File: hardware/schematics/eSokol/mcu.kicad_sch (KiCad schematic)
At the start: 16 parts, among them J1 DB25, J2 to HC-05, Q6 AO3400A, SW1 SW_LITTLE, U2 YAAJ_BluePill_SWD_Breakout, U3 TP4056, U5 AMS1117-5.0, U9 TCRT5000

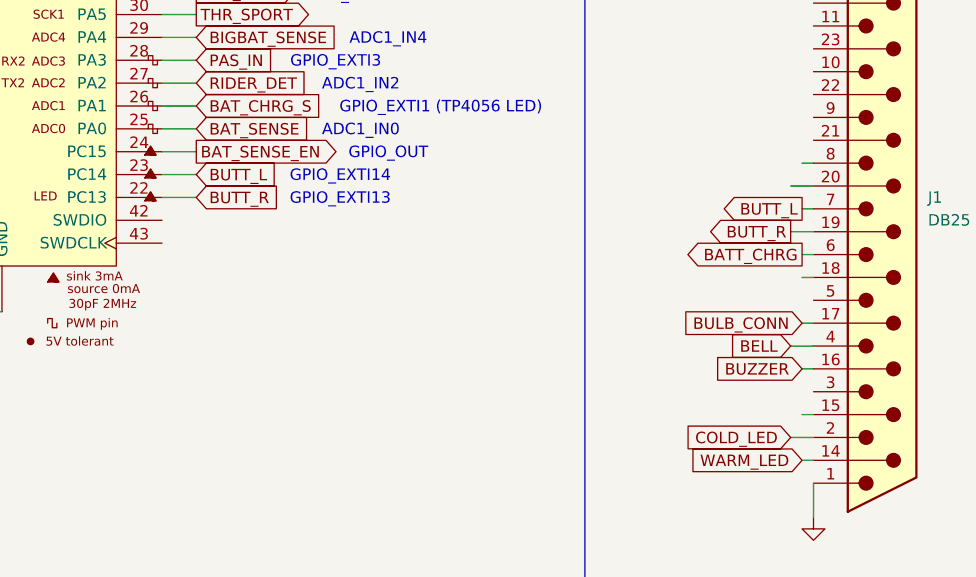
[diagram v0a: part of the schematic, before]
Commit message: Remove leftover OLED buttons
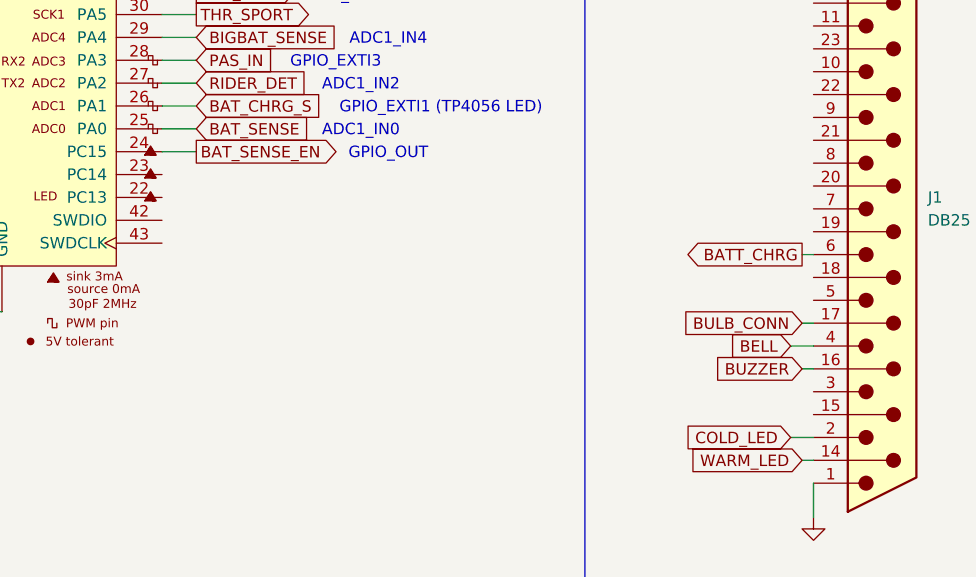
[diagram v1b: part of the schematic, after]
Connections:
- net BUTT_L: no longer names the net of J1.7
- net BUTT_L: no longer U2.23 (PC14)
- net BUTT_R: no longer names the net of J1.19 (P19)
- net BUTT_R: no longer U2.22 (PC13)
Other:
- note removed: "GPIO_EXTI14"
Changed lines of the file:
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@@
-	(wire
-		(pts
-			(xy 248.92 123.19) (xy 250.19 123.19)
-		)
-		(stroke
-			(width 0)
-			(type default)
-		)
-	)
 	(wire
 		(pts
@@
 	(wire
 		(pts
-			(xy 181.61 111.76) (xy 177.8 111.76)
-		)
-		(stroke
-			(width 0)
-			(type default)
-		)
-	)
-	(wire
-		(pts
 			(xy 135.89 111.76) (xy 137.16 111.76)
 		)
@@
 	(wire
 		(pts
-			(xy 181.61 114.3) (xy 177.8 114.3)
-		)
-		(stroke
-			(width 0)
-			(type default)
-		)
-	)
-	(wire
-		(pts
 			(xy 246.38 83.82) (xy 246.38 85.09)
 		)
@@
 	(wire
 		(pts
-			(xy 250.19 113.03) (xy 247.65 113.03)
-		)
-		(stroke
-			(width 0)
-			(type default)
-		)
-	)
-	(wire
-		(pts
 			(xy 93.98 66.04) (xy 85.09 66.04)
 		)
@@
 	(wire
 		(pts
-			(xy 248.92 138.43) (xy 250.19 138.43)
-		)
-		(stroke
-			(width 0)
-			(type default)
-		)
-	)
-	(wire
-		(pts
-			(xy 248.92 110.49) (xy 250.19 110.49)
-		)
-		(stroke
-			(width 0)
-			(type default)
-		)
-	)
-	(wire
-		(pts
 			(xy 137.16 83.82) (xy 135.89 83.82)
 		)
@@
 	(wire
 		(pts
-			(xy 250.19 115.57) (xy 248.92 115.57)
-		)
-		(stroke
-			(width 0)
-			(type default)
-		)
-	)
-	(wire
-		(pts
 			(xy 57.15 35.56) (xy 57.15 34.29)
 		)
@@
 		(pts
 			(xy 177.8 88.9) (xy 181.61 88.9)
-		)
-		(stroke
-			(width 0)
-			(type default)
-		)
-	)
-	(wire
-		(pts
-			(xy 250.19 118.11) (xy 247.65 118.11)
 		)
 		(stroke
@@
 		)
 	)
-	(text "GPIO_EXTI13"
-		(exclude_from_sim no)
-		(at 197.612 114.554 0)
-		(effects
-			(font
-				(size 1.27 1.27)
-			)
-		)
-	)
 	(text "ADC1_IN4\n"
 		(exclude_from_sim no)
@@
 		(exclude_from_sim no)
 		(at 118.872 81.788 0)
-		(effects
-			(font
-				(size 1.27 1.27)
-			)
-		)
-	)
-	(text "GPIO_EXTI14"
-		(exclude_from_sim no)
-		(at 197.612 112.014 0)
 		(effects
 			(font
@@
 		)
 	)
-	(global_label "BUTT_R"
-		(shape output)
-		(at 247.65 118.11 180)
-		(fields_autoplaced yes)
-		(effects
-			(font
-				(size 1.27 1.27)
-			)
-			(justify right)
-		)
-		(property "Intersheetrefs" "${INTERSHEET_REFS}"
-			(at 237.8915 118.11 0)
-			(effects
-				(font
-					(size 1.27 1.27)
-				)
-				(justify right)
-				(hide yes)
-			)
-		)
-	)
 	(global_label "BT_RX"
 		(shape input)
@@
 				)
 				(justify right)
-				(hide yes)
-			)
-		)
-	)
-	(global_label "BUTT_R"
-		(shape input)
-		(at 181.61 114.3 0)
-		(fields_autoplaced yes)
-		(effects
-			(font
-				(size 1.27 1.27)
-			)
-			(justify left)
-		)
-		(property "Intersheetrefs" "${INTERSHEET_REFS}"
-			(at 191.3685 114.3 0)
-			(effects
-				(font
-					(size 1.27 1.27)
-				)
-				(justify left)
 				(hide yes)
 			)
@@
 		)
 	)
-	(global_label "BUTT_L"
-		(shape input)
-		(at 181.61 111.76 0)
-		(fields_autoplaced yes)
-		(effects
-			(font
-				(size 1.27 1.27)
-			)
-			(justify left)
-		)
-		(property "Intersheetrefs" "${INTERSHEET_REFS}"
-			(at 191.1266 111.76 0)
-			(effects
-				(font
-					(size 1.27 1.27)
-				)
-				(justify left)
-				(hide yes)
-			)
-		)
-	)
 	(global_label "BUZZER"
 		(shape input)
@@
 			(effects
 				(font
-					(size 1.27 1.27)
-				)
-				(justify right)
-				(hide yes)
-			)
-		)
-	)
-	(global_label "BUTT_L"
-		(shape output)
-		(at 248.92 115.57 180)
-		(fields_autoplaced yes)
-		(effects
-			(font
-				(size 1.27 1.27)
-			)
-			(justify right)
-		)
-		(property "Intersheetrefs" "${INTERSHEET_REFS}"
-			(at 239.4034 115.57 0)
-			(effects
-				(font

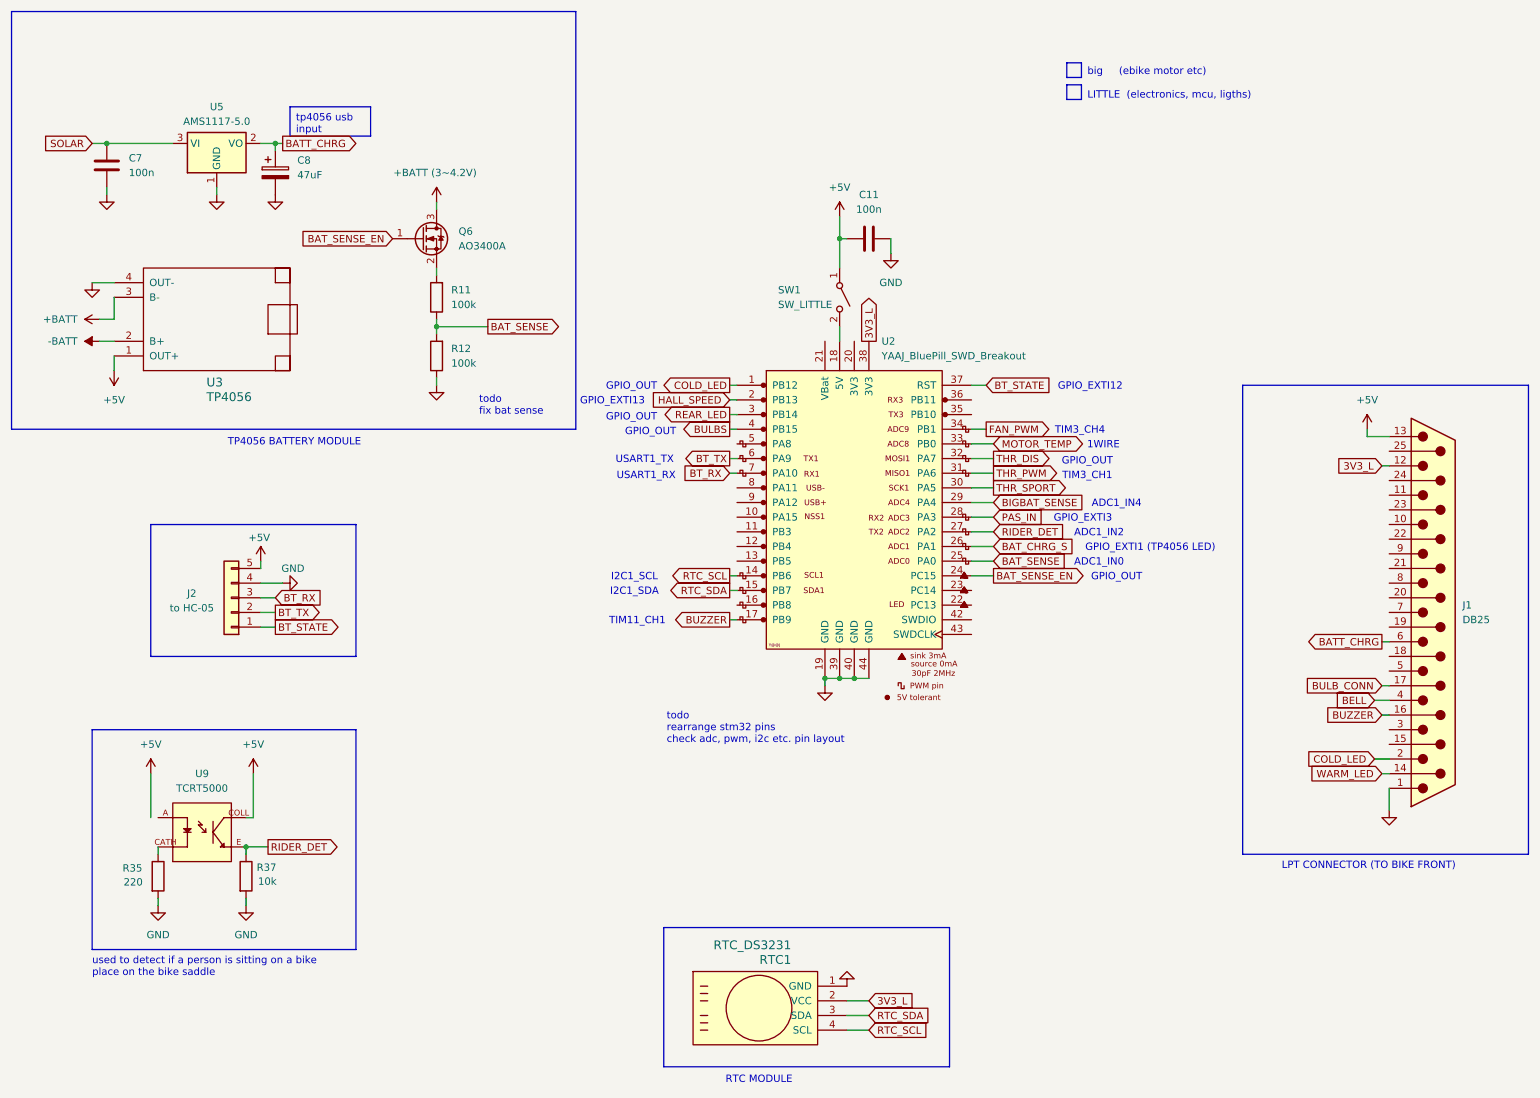
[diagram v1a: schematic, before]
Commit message: hardware/schematics: update mcu and big schematics to reflect current project state
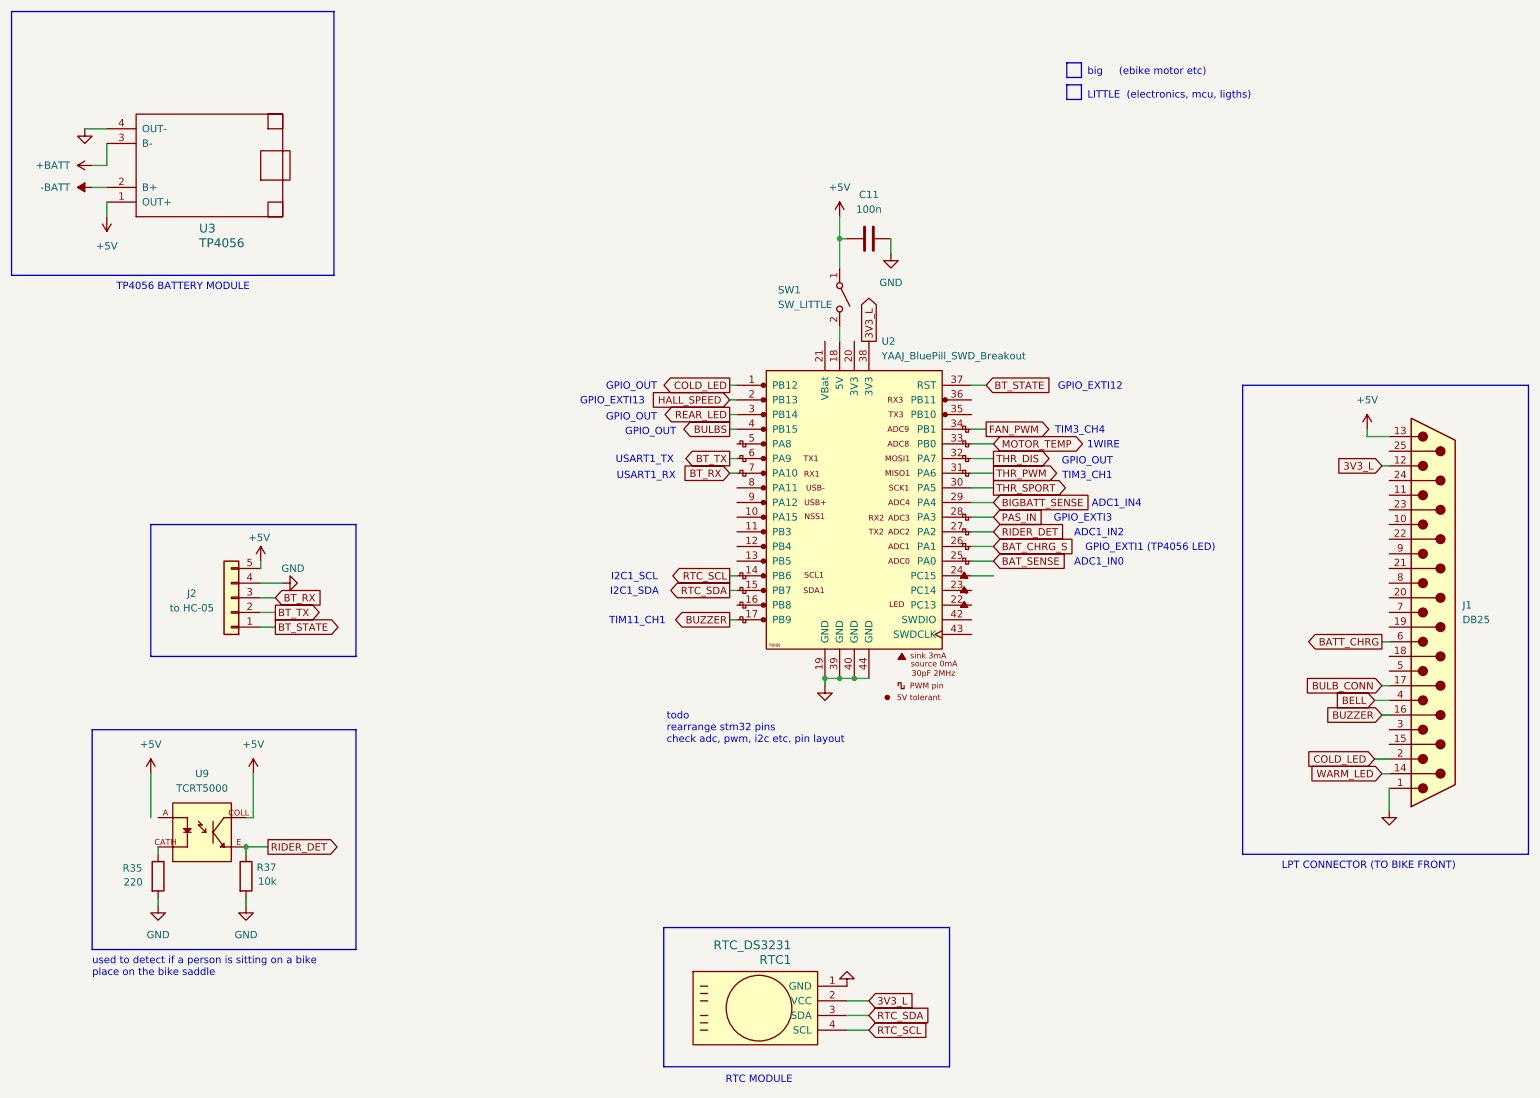
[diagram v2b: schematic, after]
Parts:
- removed C7: 100n, symbol Device:C
- removed C8: 47uF, symbol Device:C_Polarized
- removed Q6: AO3400A, Package_TO_SOT_SMD:SOT-23, symbol Transistor_FET:AO3400A
- removed R11, R12: 100k, symbol Device:R
- removed U5: AMS1117-5.0, Package_TO_SOT_SMD:SOT-223-3_TabPin2, symbol Regulator_Linear:AMS1117-5.0
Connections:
- net BAT_SENSE_EN: no longer names the net of U2.24 (PC15)
- net BIGBAT_SENSE renamed BIGBATT_SENSE
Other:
- note removed: "todo fix bat sense"
- moved on the sheet: U3

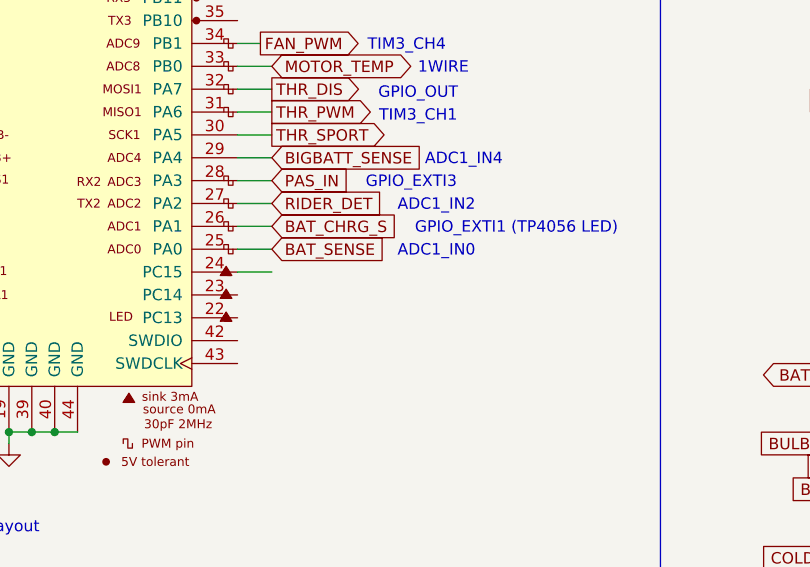
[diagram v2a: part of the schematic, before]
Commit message: hardware/schematics: add initial blinkers and brake handler circuits
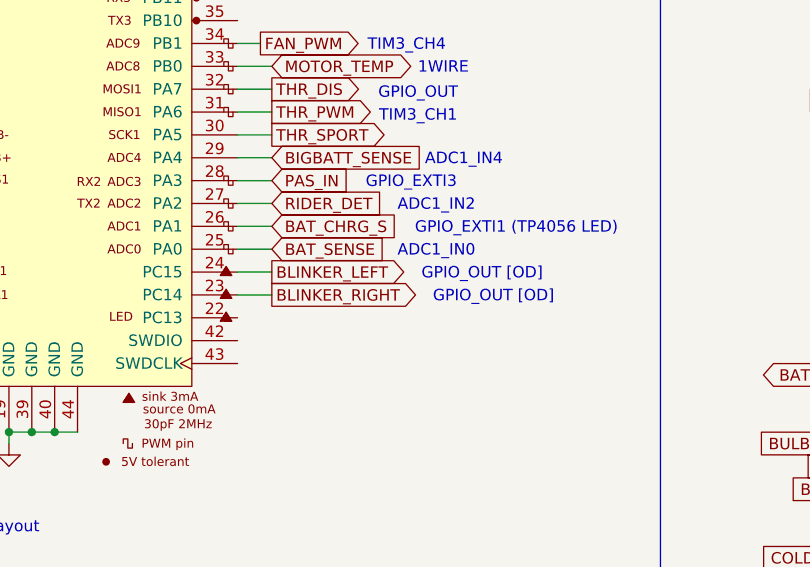
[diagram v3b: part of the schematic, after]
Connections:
- net BLINKER_RIGHT: now reaches U2.23 (PC14)
- net BLINKER_LEFT: now reaches U2.24 (PC15)
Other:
- note added: "GPIO_OUT [OD]"
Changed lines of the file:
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@@
+	(wire
+		(pts
+			(xy 181.61 111.76) (xy 177.8 111.76)
+		)
+		(stroke
+			(width 0)
+			(type default)
+		)
+	)
 	(wire
 		(pts
@@
 		)
 	)
+	(text "GPIO_OUT [OD]\n"
+		(exclude_from_sim no)
+		(at 204.978 109.474 0)
+		(effects
+			(font
+				(size 1.27 1.27)
+			)
+		)
+	)
 	(text "ADC1_IN4\n"
 		(exclude_from_sim no)
@@
 			)
 			(justify left)
+		)
+	)
+	(text "GPIO_OUT [OD]"
+		(exclude_from_sim no)
+		(at 206.248 112.014 0)
+		(effects
+			(font
+				(size 1.27 1.27)
+			)
 		)
 	)
@@
 		)
 	)
+	(global_label "BLINKER_LEFT"
+		(shape output)
+		(at 181.61 109.22 0)
+		(fields_autoplaced yes)
+		(effects
+			(font
+				(size 1.27 1.27)
+			)
+			(justify left)
+		)
+		(property "Intersheetrefs" "${INTERSHEET_REFS}"
+			(at 197.7185 109.22 0)
+			(effects
+				(font
+					(size 1.27 1.27)
+				)
+				(justify left)
+				(hide yes)
+			)
+		)
+	)
 	(global_label "BUZZER"
 		(shape output)
@@
 				(hide yes)
 			)
+		)
+	)
+	(global_label "BLINKER_RIGHT"
+		(shape output)
+		(at 181.61 111.76 0)
+		(fields_autoplaced yes)
+		(effects
+			(font
+				(size 1.27 1.27)
+			)
+			(justify left)
+		)
+		(property "Intersheetrefs" "${INTERSHEET_REFS}"
+			(at 198.9281 111.76 0)
+			(effects
+				(font
+					(size 1.27 1.27)
+				)
+				(justify left)
+				(hide yes)
+			)
